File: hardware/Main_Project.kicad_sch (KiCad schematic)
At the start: 53 parts, among them J1 A_Motor, J2 B_Motor, J3 Power_Outputs, U1 L7805, U2 L298N, U4 L298N

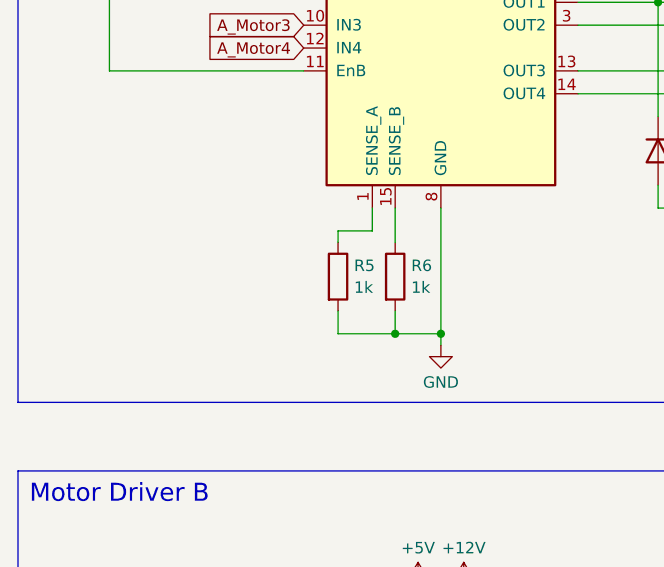
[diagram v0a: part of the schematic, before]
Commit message: changed resistor values
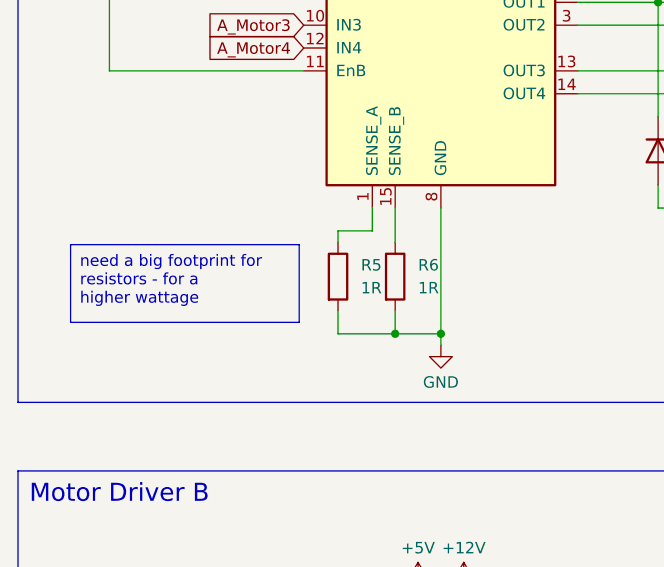
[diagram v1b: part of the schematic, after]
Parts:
- R5, R6: value 1k -> 1R
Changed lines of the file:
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@@
     (effects (font (size 1.27 1.27)) (justify top))
+  )
+  (text_box "need a big footprint for resistors - for a higher wattage"
+    (at 24.892 178.054 0) (size 25.4 8.636)
+    (stroke (width 0) (type default))
+    (fill (type none))
+    (effects (font (size 1.27 1.27)) (justify left top))
   )
   (text "5V Regulator" (at 20.32 71.12 0)
@@
   (symbol (lib_id "Device:R") (at 54.61 181.61 0) (unit 1)
     (in_bom yes) (on_board yes) (dnp no) (fields_autoplaced)
-    (property "Reference" "R5" (at 56.388 180.3979 0)
-      (effects (font (size 1.27 1.27)) (justify left))
-    )
-    (property "Value" "1k" (at 56.388 182.8221 0)
+    (property "Reference" "R5" (at 57.15 180.34 0)
+      (effects (font (size 1.27 1.27)) (justify left))
+    )
+    (property "Value" "1R" (at 57.15 182.88 0)
       (effects (font (size 1.27 1.27)) (justify left))
     )
@@
   (symbol (lib_id "Device:R") (at 60.96 181.61 0) (unit 1)
     (in_bom yes) (on_board yes) (dnp no) (fields_autoplaced)
-    (property "Reference" "R6" (at 62.738 180.3979 0)
-      (effects (font (size 1.27 1.27)) (justify left))
-    )
-    (property "Value" "1k" (at 62.738 182.8221 0)
-      (effects (font (size 1.27 1.27)) (justify left))
-    )
+    (property "Reference" "R6" (at 63.5 180.34 0)
+      (effects (font (size 1.27 1.27)) (justify left))
+    )
+    (property "Value" "1R" (at 63.5 182.88 0)
+      (effects (font (size 1.27 1.27)) (justify left))
+    )
